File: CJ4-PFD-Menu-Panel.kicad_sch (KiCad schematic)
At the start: 0 parts

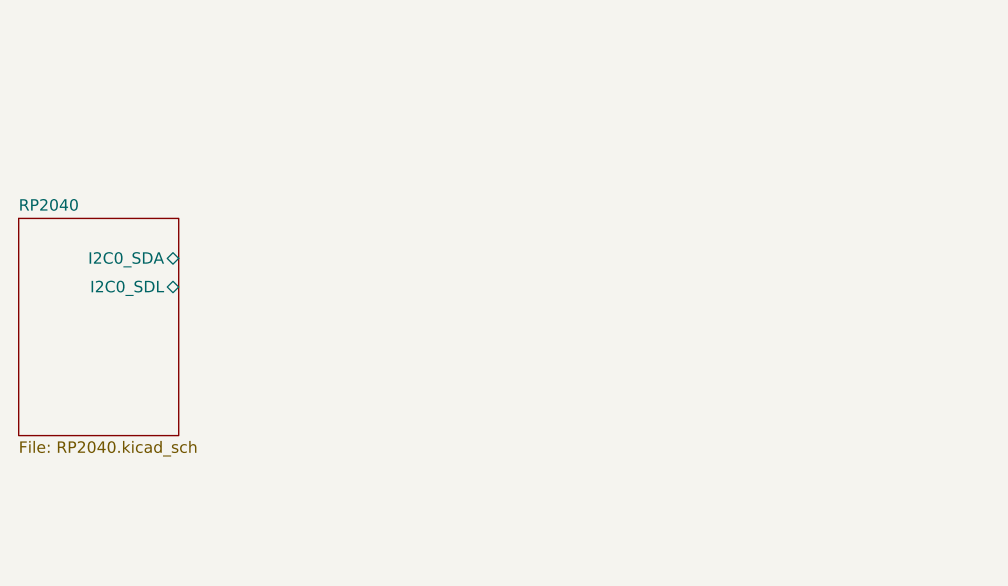
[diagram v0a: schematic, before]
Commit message: Add TCA8418
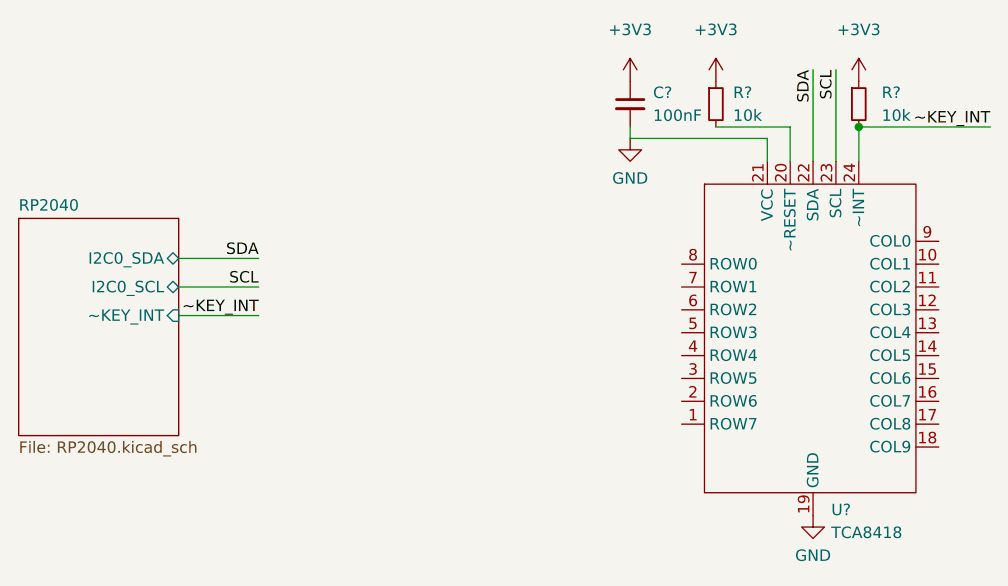
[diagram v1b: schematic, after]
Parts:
- added C?: 100nF, symbol Device:C_Small
- added R? (x2): 10k, symbol Device:R_Small
- added U?: TCA8418, Package_DFN_QFN:WQFN-24-1EP_4x4mm_P0.5mm_EP2.6x2.6mm, symbol Custom_Symbols:TCA8418
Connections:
- new net: R?.2, U?.20 (~RESET)
- new net +3V3: C?.1, R?.1, R?.1
- new net GND: C?.2, U?.19 (GND), U?.21 (VCC)
- new net SCL: U?.23 (SCL)
- new net SDA: U?.22 (SDA)
- new net ~KEY_INT: R?.2, U?.24 (~INT)
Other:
- sheet RP2040 ports: added I2C0_SCL, ~KEY_INT; removed I2C0_SDL

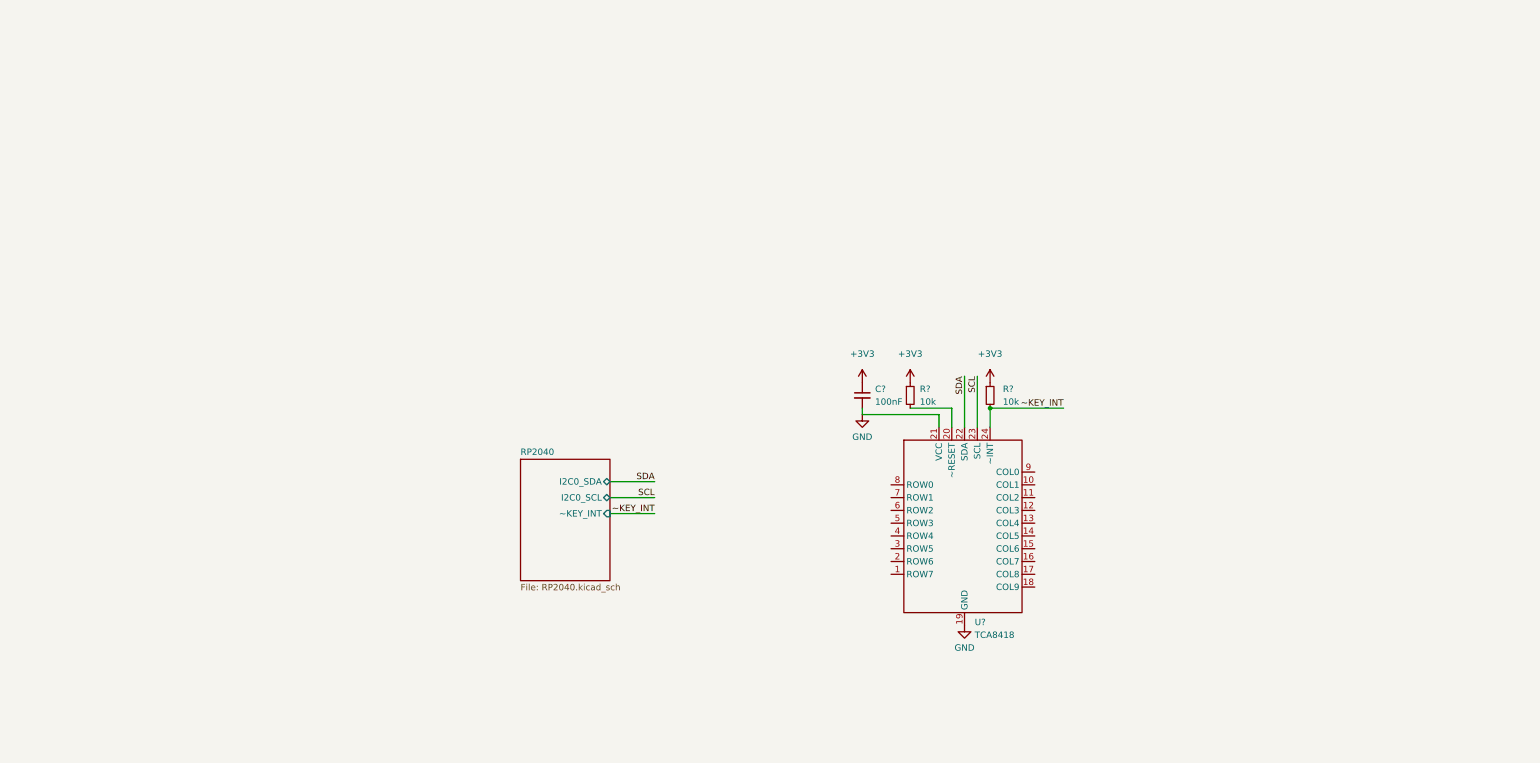
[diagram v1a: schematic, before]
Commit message: Expose the GPIO pins
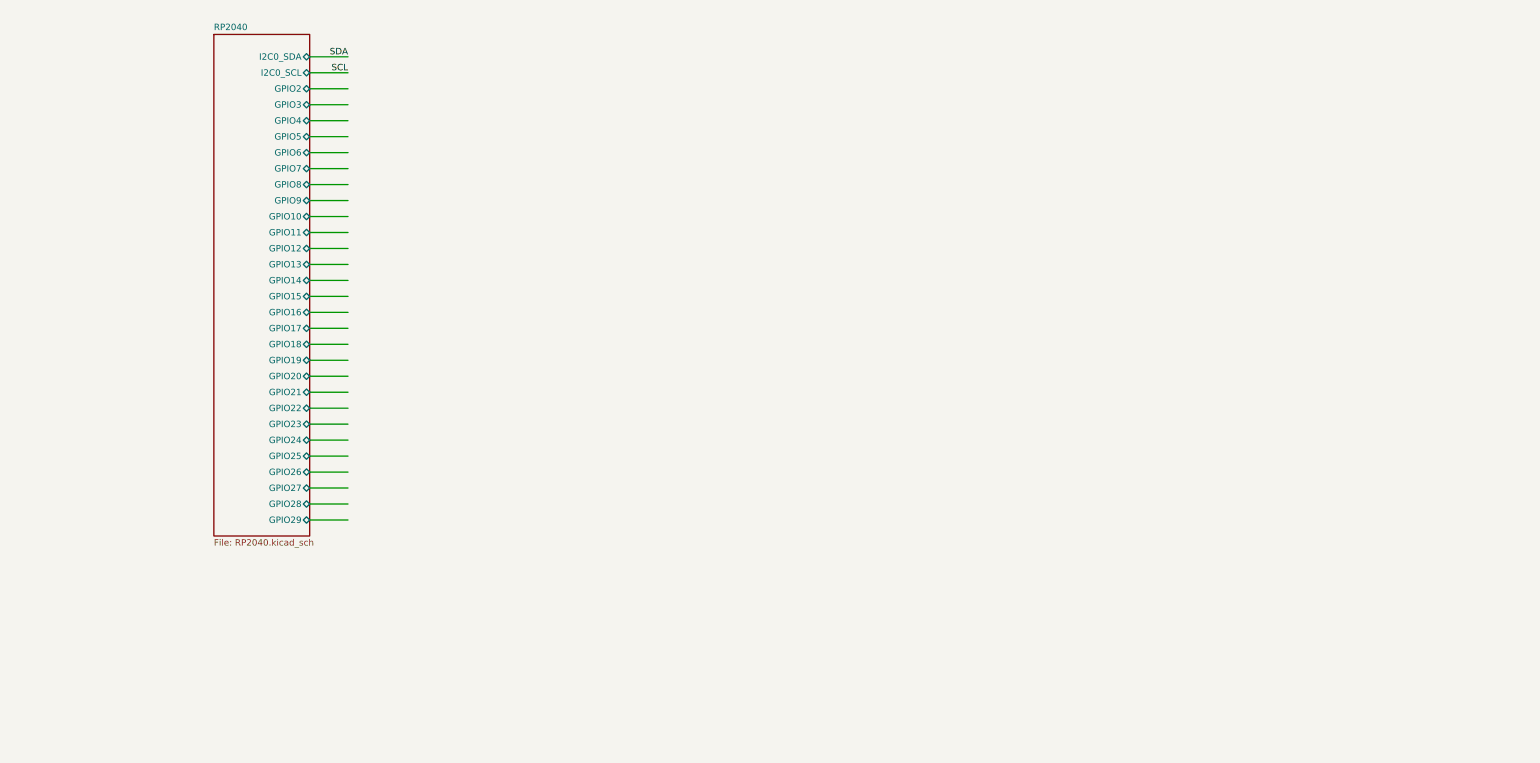
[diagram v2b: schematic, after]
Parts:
- removed C?: 100nF, symbol Device:C_Small
- removed R? (x2): 10k, symbol Device:R_Small
- removed U?: TCA8418, Package_DFN_QFN:WQFN-24-1EP_4x4mm_P0.5mm_EP2.6x2.6mm, symbol Custom_Symbols:TCA8418
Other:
- sheet RP2040 ports: added GPIO10, GPIO11, GPIO12, GPIO13, GPIO14, GPIO15, GPIO16, GPIO17, GPIO18, GPIO19, GPIO2, GPIO20, GPIO21, GPIO22, GPIO23, GPIO24, GPIO25, GPIO26, GPIO27, GPIO28, GPIO29, GPIO3, GPIO4, GPIO5, GPIO6, GPIO7, GPIO8, GPIO9; removed ~KEY_INT

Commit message: Buttons and LED driver
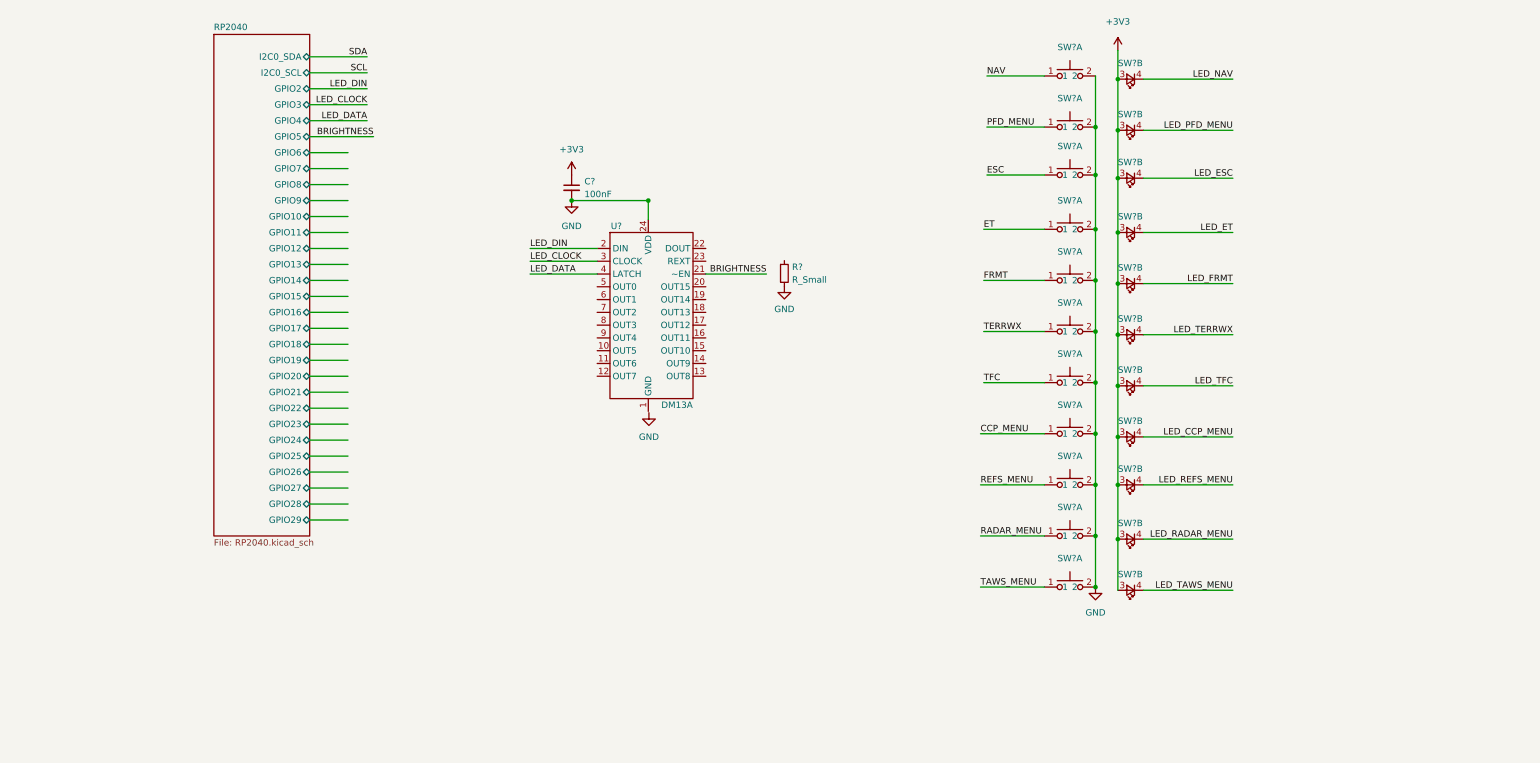
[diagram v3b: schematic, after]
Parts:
- added C?: 100nF, symbol Device:C_Small
- added R?: R_Small, symbol Device:R_Small
- added SW? (x22): SW_PUSH_LED, Custom_Footprints:SW_PUSH_LED, symbol Custom_Symbols:SW_PUSH_LED
- added U?: DM13A, Package_SO:SSOP-24_3.9x8.7mm_P0.635mm, symbol Custom_Symbols:DM13A
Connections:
- new net +3V3: C?.1, SW?.3, SW?.3, SW?.3, SW?.3, SW?.3, SW?.3, SW?.3, SW?.3, SW?.3, SW?.3, SW?.3
- new net BRIGHTNESS: U?.21 (~EN)
- new net CCP_MENU: SW?.1
- new net ESC: SW?.1
- new net ET: SW?.1
- new net FRMT: SW?.1
- new net GND: C?.2, R?.2, SW?.2, SW?.2, SW?.2, SW?.2, SW?.2, SW?.2, SW?.2, SW?.2, SW?.2, SW?.2, SW?.2, U?.24 (VDD)
- new net LED_CCP_MENU: SW?.4
- new net LED_CLOCK: U?.3 (CLOCK)
- new net LED_DATA: U?.4 (LATCH)
- new net LED_DIN: U?.2 (DIN)
- new net LED_ESC: SW?.4
- new net LED_ET: SW?.4
- new net LED_FRMT: SW?.4
- new net LED_NAV: SW?.4
- new net LED_PFD_MENU: SW?.4
- new net LED_RADAR_MENU: SW?.4
- new net LED_REFS_MENU: SW?.4
- new net LED_TAWS_MENU: SW?.4
- new net LED_TERRWX: SW?.4
- new net LED_TFC: SW?.4
- new net NAV: SW?.1
- new net PFD_MENU: SW?.1
- new net RADAR_MENU: SW?.1
- new net REFS_MENU: SW?.1
- new net TAWS_MENU: SW?.1
- new net TERRWX: SW?.1
- new net TFC: SW?.1

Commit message: Initial schematic complete
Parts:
- added H1, H2, H3, H4: Board mount, MountingHole:MountingHole_3.2mm_M3, symbol Mechanical:MountingHole
- added H10, H8, H9: JLCPCB tooling, Custom_Footprints:JLCPCB_Tooling_Hole, symbol Mechanical:MountingHole
- added H5: BARO encoder, Custom_Footprints:EN11-HSM1BF20 panel mount, symbol Mechanical:MountingHole
- added H6: MENU ADV and DATA encoder, Custom_Footprints:EC11E-BB24C03_PM, symbol Mechanical:MountingHole
- added H7: TILT and RANGE encoder, Custom_Footprints:EC11E-BB24C03_PM, symbol Mechanical:MountingHole
- added J3: BARO encoder, Connector_JST:JST_XH_B5B-XH-A_1x05_P2.50mm_Vertical, symbol Connector_Generic:Conn_01x05
- added J4: MENU ADV and DATA encoder, Connector_JST:JST_XH_B8B-XH-A_1x08_P2.50mm_Vertical, symbol Connector_Generic:Conn_01x08
- added J5: TILT and RANGE encoder, Connector_JST:JST_XH_B8B-XH-A_1x08_P2.50mm_Vertical, symbol Connector_Generic:Conn_01x08
- added SW14, SW15: SW_Push, symbol Switch:SW_Push
- added TP1, TP2, TP3, TP4, TP5: TestPoint, TestPoint:TestPoint_Keystone_5000-5004_Miniature, symbol Connector:TestPoint
- C1: renamed from C?; footprint (none) -> Custom_Footprints:Perfect_0402
- R7: renamed from R?; footprint (none) -> Custom_Footprints:Perfect_0402
- gave numbers to parts that had none: 12
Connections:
- net BRIGHTNESS: now also TP4.1
- net GND: now also U2.1 (GND), J3.2 (Pin_2), J3.5 (Pin_5), J4.6 (Pin_6), J4.7 (Pin_7), J5.6 (Pin_6), J5.7 (Pin_7), SW14.2, SW15.2, TP5.1
- net LED_CCP_MENU: now also U2.12 (OUT7)
- net LED_CLOCK: now also TP2.1
- net LED_DIN: now also TP1.1
- net LED_ESC: now also U2.7 (OUT2)
- net LED_ET: now also U2.8 (OUT3)
- net LED_FRMT: now also U2.9 (OUT4)
- net LED_NAV: now also U2.5 (OUT0)
- net LED_PFD_MENU: now also U2.6 (OUT1)
- net LED_RADAR_MENU: now also U2.14 (OUT9)
- net LED_REFS_MENU: now also U2.15 (OUT10)
- net LED_TAWS_MENU: now also U2.13 (OUT8)
- net LED_TERRWX: now also U2.10 (OUT5)
- net LED_TFC: now also U2.11 (OUT6)
- net at R7.1: now also U2.23 (REXT)
- net LED_MASTER_CAUTION: now reaches U2.16 (OUT11)
- net LED_MASTER_WARNING: now reaches U2.17 (OUT12)
- net LED_DATA renamed LED_LATCH
- net LED_LATCH: now also TP3.1
- new net AUTO_TILT_BTN: J5.5 (Pin_5)
- new net BARO_A: J3.1 (Pin_1)
- new net BARO_B: J3.4 (Pin_4)
- new net DATA_A: J4.3 (Pin_3)
- new net DATA_B: J4.4 (Pin_4)
- new net MASTER_CAUTION: SW15.1
- new net MASTER_WARNING: SW14.1
- new net MENU_ADV_A: J4.1 (Pin_1)
- new net MENU_ADV_B: J4.2 (Pin_2)
- new net RANGE_A: J5.3 (Pin_3)
- new net RANGE_B: J5.4 (Pin_4)
- new net SELECT_BTN: J4.5 (Pin_5)
- new net STD_BTN: J3.3 (Pin_3)
- new net TILT_A: J5.1 (Pin_1)
- new net TILT_B: J5.2 (Pin_2)
- no-connect marks 0 -> 6
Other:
- sheet RP2040 ports: added GPIO0, GPIO1; removed I2C0_SCL, I2C0_SDA
- note added: "Backlight LED controller"
- note added: "Buttons and backlights"
- note added: "Encoder connectors"
- note added: "Microcontroller"
- note added: "Mounting and tooling holes"
- note added: "Test points"
- moved on the sheet: C1, R7, SW10A, SW10B, SW11A, SW11B, SW12A, SW12B, SW13A, SW13B, SW3A, SW3B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

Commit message: More updates
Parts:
- removed SW14, SW15: SW_Push, symbol Switch:SW_Push
- added J6, J7: Conn_01x02, Connector_JST:JST_XH_B2B-XH-A_1x02_P2.50mm_Vertical, symbol Connector_Generic:Conn_01x02
- SW10, SW11, SW12, SW13, SW3, SW4, SW5, SW6, SW7, SW8, SW9: footprint Custom_Footprints:SW_PUSH_LED -> Custom_Footprints:SW_PUSH_LED_SMD
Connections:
- net GND: now also J6.2 (Pin_2), J7.2 (Pin_2)
- net MASTER_CAUTION: now also J7.1 (Pin_1)
- net MASTER_WARNING: now also J6.1 (Pin_1)
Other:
- note added: "External button connections"

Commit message: Some board layout work
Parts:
- H5: footprint Custom_Footprints:EN11-HSM1BF20 panel mount -> Custom_Footprints:EN11-HSM1BF20_PM
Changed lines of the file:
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@@
       (effects (font (size 1.27 1.27)) (justify left))
     )
-    (property "Footprint" "Custom_Footprints:EN11-HSM1BF20 panel mount" (id 2) (at 212.09 19.685 0)
+    (property "Footprint" "Custom_Footprints:EN11-HSM1BF20_PM" (id 2) (at 212.09 19.685 0)
       (effects (font (size 1.27 1.27)) hide)
     )
@@
     )
     (path "/fbf71956-95c2-45ee-90f3-fa3bc70be935"
-      (reference "H5") (unit 1) (value "BARO encoder") (footprint "Custom_Footprints:EN11-HSM1BF20 panel mount")
+      (reference "H5") (unit 1) (value "BARO encoder") (footprint "Custom_Footprints:EN11-HSM1BF20_PM")
     )
     (path "/0d7d212f-72a7-4686-8e1c-59df833b2d14"
@@
     )
     (path "/f2c43eeb-76da-49f4-b8e6-cd74ebb3190b/4553d9ef-e5ac-4c89-b061-b30ba60abcbd"
-      (reference "SW1") (unit 1) (value "SW_Push") (footprint "Button_Switch_SMD:SW_Push_1P1T_NO_6x6mm_H9.5mm")
+      (reference "SW1") (unit 1) (value "SW_Push") (footprint "Button_Switch_SMD:SW_SPST_TL3342")
     )
     (path "/f2c43eeb-76da-49f4-b8e6-cd74ebb3190b/0692de5f-2423-4dd0-a07b-d18c34284fdf"
-      (reference "SW2") (unit 1) (value "SW_Push") (footprint "Button_Switch_SMD:SW_Push_1P1T_NO_6x6mm_H9.5mm")
+      (reference "SW2") (unit 1) (value "SW_Push") (footprint "Button_Switch_SMD:SW_SPST_TL3342")
     )
     (path "/f541c5dd-6c97-4713-864b-de0d8fcb1e48"
